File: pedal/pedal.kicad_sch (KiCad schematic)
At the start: 55 parts, among them J1 AudioJack3, J2 AudioJack3, J3 Micro SD, J4 USB_B_Micro, J5 Debug, U1 LP2985-1.8, U2 PCM3060, U3 TPS62172DSG, U4 TL072, U5 STM32H750IBTx, U6 RC4580, Y1 25MHz

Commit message: update JOURNAL and step down BC
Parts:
- added C37: 100nF, symbol Device:C
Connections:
- net +3V3: no longer C1.1, C10.2, C11.2, C12.2, C13.2, C14.2, C15.2, C16.2, C17.2, C2.1, C21.2, C24.1, C25.1, C26.2, C27.2, C28.2, C29.2, C3.2, C30.1, C30.2, C33.2, C34.2, C4.2, C5.2, C6.2, C7.2, C8.2, C9.2, J4.5 (GND), QSPI.10 (GND), SDRAM.12 (GNDQ), SDRAM.28 (GND), SDRAM.41 (GND), SDRAM.46 (GNDQ), SDRAM.52 (GNDQ), SDRAM.54 (GND), SDRAM.6 (GNDQ), U1.2 (GND), U2.8 (DGND), U3.1 (PGND), U3.2 (VIN), U3.3 (EN), U3.4 (AGND), U3.5 (FB), U5.102 (VSS), U5.113 (VSS), U5.126 (VSS), U5.135 (VSS), U5.14 (VSS), U5.148 (VSS), U5.158 (VSS), U5.22 (VSS), U5.48 (VSS), U5.61 (VSS), U5.71 (VSS), U5.90 (VSS)
- net at U2.21 (V_{COM}): now also C37.1
- net GNDA renamed +9V
- net +9V: now also C29.2, C30.1, C30.2, U3.1 (PGND), U3.2 (VIN), U3.3 (EN), U3.4 (AGND), U3.5 (FB), C37.2
- new net GNDD: C1.1, C10.2, C11.2, C12.2, C13.2, C14.2, C15.2, C16.2, C17.2, C2.1, C21.2, C24.1, C25.1, C26.2, C27.2, C28.2, C3.2, C33.2, C34.2, C4.2, C5.2, C6.2, C7.2, C8.2, C9.2, J4.5 (GND), QSPI.10 (GND), SDRAM.12 (GNDQ), SDRAM.28 (GND), SDRAM.41 (GND), SDRAM.46 (GNDQ), SDRAM.52 (GNDQ), SDRAM.54 (GND), SDRAM.6 (GNDQ), U1.2 (GND), U2.8 (DGND), U5.102 (VSS), U5.113 (VSS), U5.126 (VSS), U5.135 (VSS), U5.14 (VSS), U5.148 (VSS), U5.158 (VSS), U5.22 (VSS), U5.48 (VSS), U5.61 (VSS), U5.71 (VSS), U5.90 (VSS)
- no-connect marks 1 -> 3
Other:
- moved on the sheet: J3, J4, J5, L1, U1, U2, U3

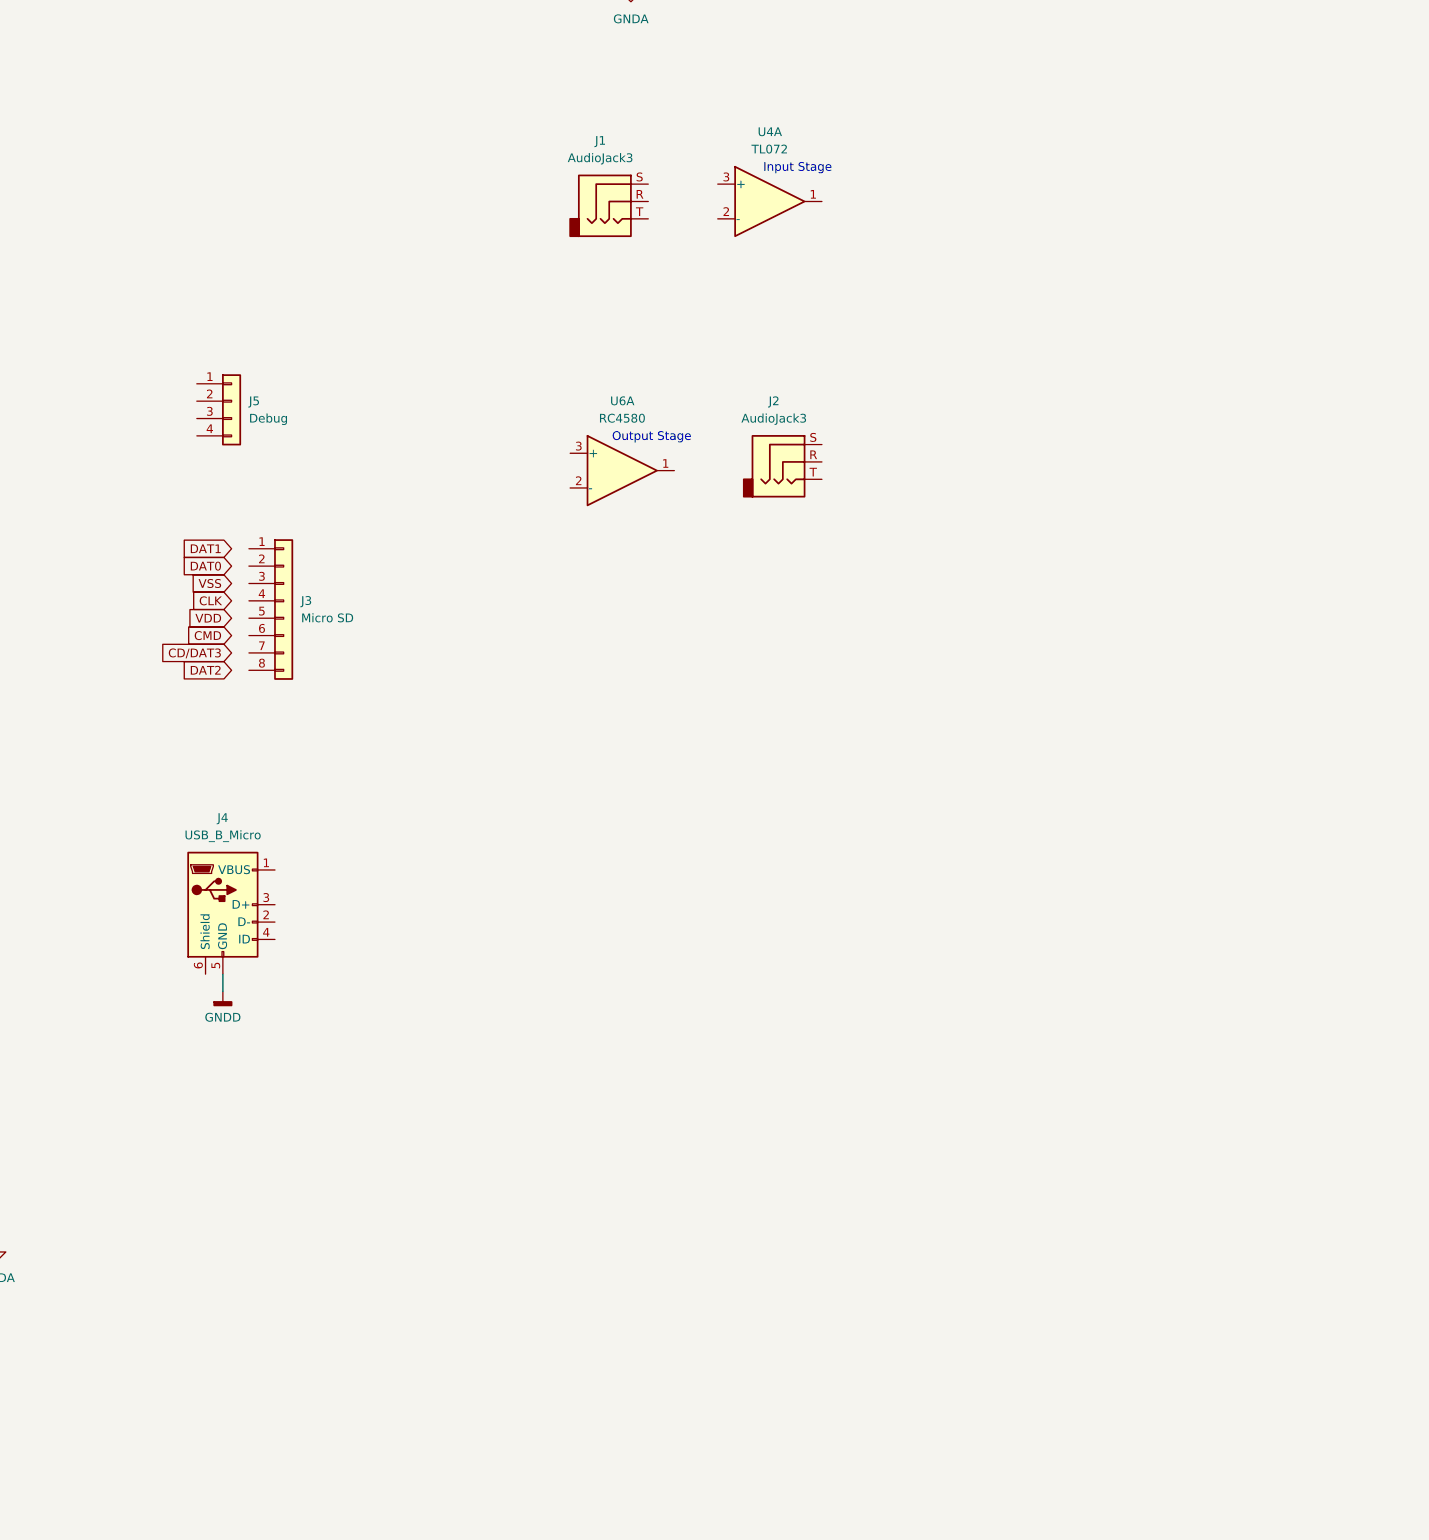
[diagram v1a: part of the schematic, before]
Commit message: consider differential inputs and outputs
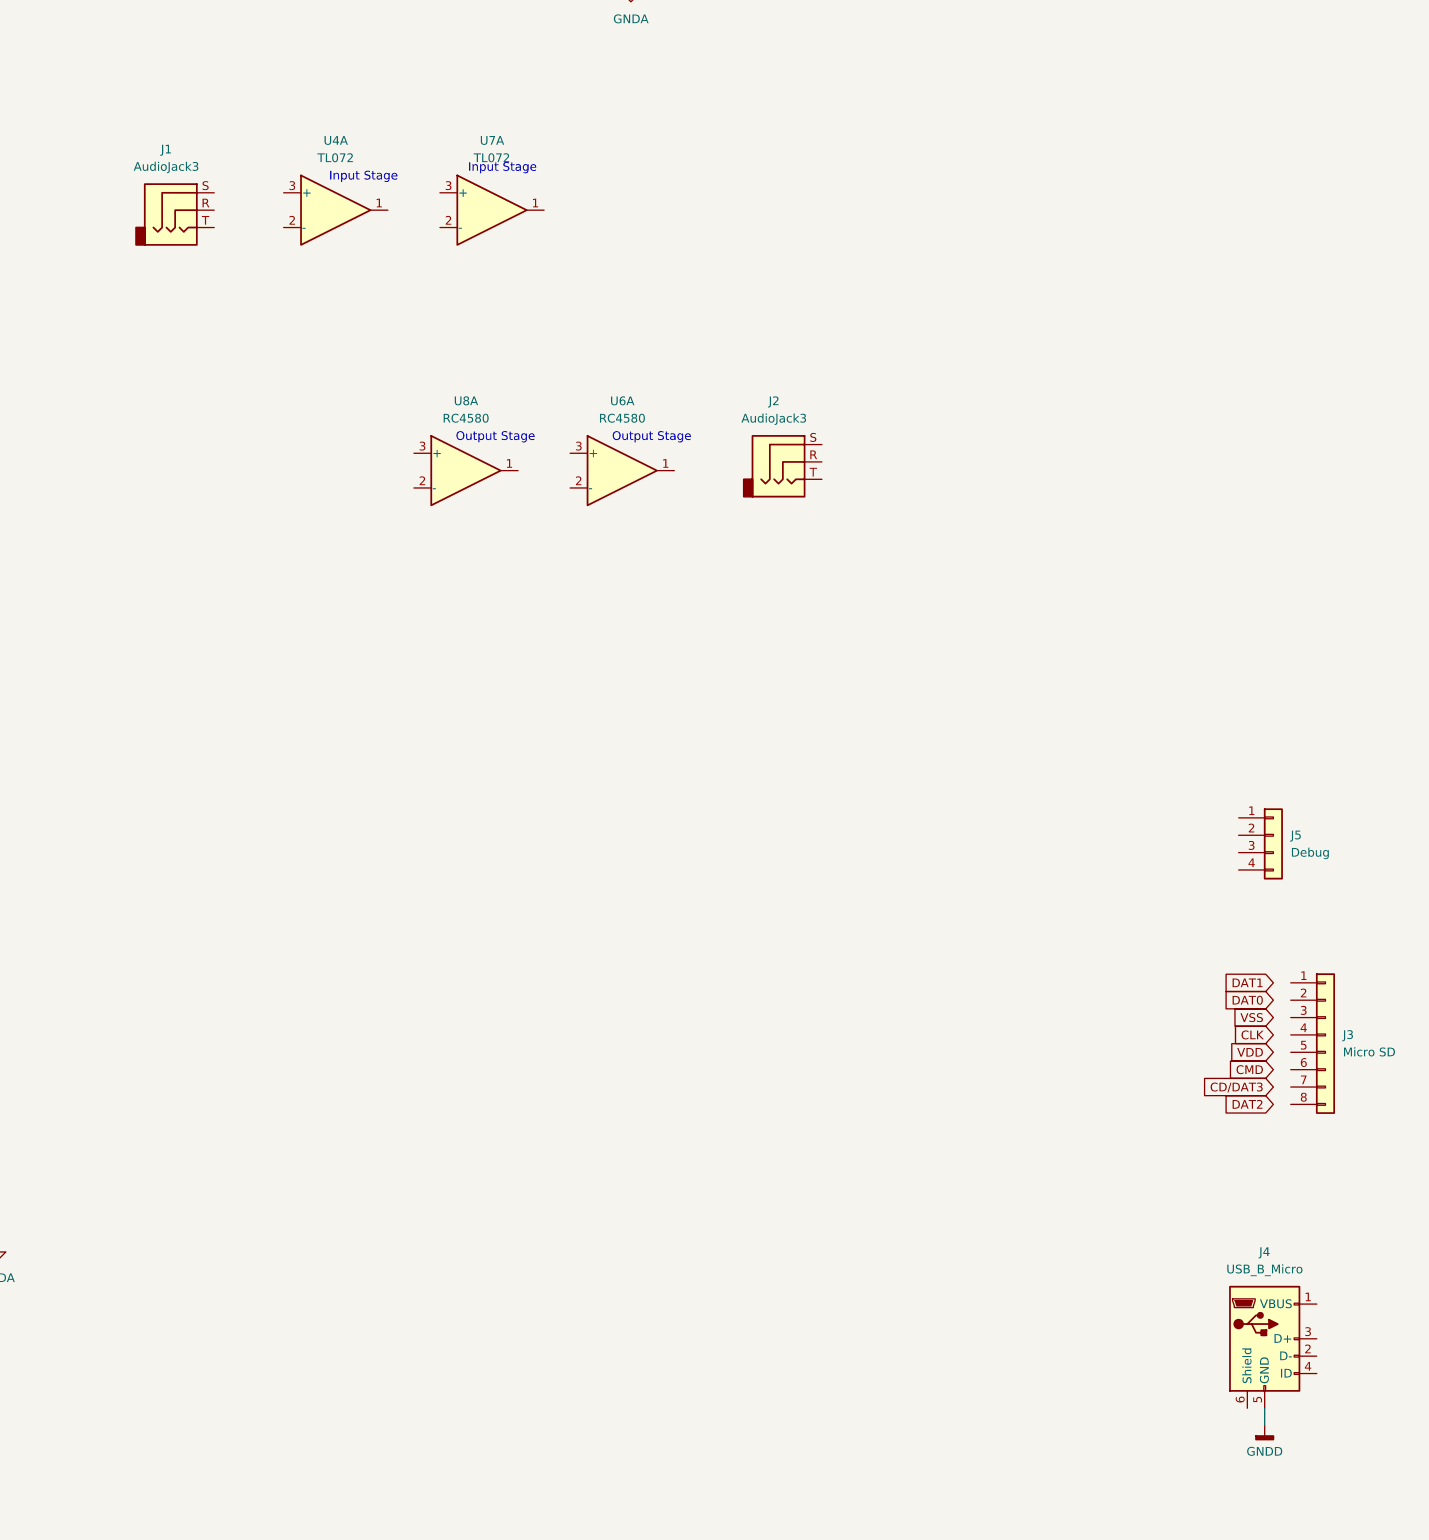
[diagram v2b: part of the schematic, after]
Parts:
- added U7: TL072, symbol Amplifier_Operational:TL072
- added U8: RC4580, symbol Amplifier_Operational:RC4580
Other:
- moved on the sheet: J1, J3, J4, J5, U4A

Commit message: Update simulation & dual op amps
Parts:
- removed U4, U7: TL072, symbol Amplifier_Operational:TL072
- removed U6: RC4580, symbol Amplifier_Operational:RC4580
- added C38: 1uF, symbol Device:C
- added C39, C40: 4.7uF, symbol Device:C
- added C41, C44: 10uF, symbol Device:C
- added C42: 2.2uF, symbol Device:C
- added C43: 10nF, symbol Device:C
- added C45: 330pF, symbol Device:C
- added C46: 0.1uF, symbol Device:C
- added C47: C, symbol Device:C
- added R10, R11, R14, R5: R, symbol Device:R
- added R12: 20k, symbol Device:R
- added R13, R6, R8: 10k, symbol Device:R
- added R4: 1k, symbol Device:R
- added R7, R9: 820, symbol Device:R
- added U4: LM27761, Package_SON:WSON-8-1EP_2x2mm_P0.5mm_EP0.9x1.6mm, symbol Regulator_SwitchedCapacitor:LM27761
- added U6: TL072, symbol Amplifier_Operational:TL072
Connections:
- net +3V3: no longer C35.1, C36.1, U2.24 (V_{CC})
- net +9V: now also J1.S, C39.2, C40.2, C41.1, C42.2, C46.2, R11.2, U4.2 (GND)
- net at U8.1: now also R5.1
- net at U8.2 (-): now also R9.2
- net at U8.3 (+): now also R7.2
- net INPUT: now reaches J1.T
- net INPUT: now also C47.1
- net at C37.1, U2.21 (V_{COM}): now also C41.2
- net VoutL-: now reaches U2.19 (V_{OUT}L-)
- net VoutL-: now also R6.1
- net VoutL+: now reaches U2.20 (V_{OUT}L+)
- net VoutL+: now also R8.1
- net VinL: now reaches U2.25 (V_{IN}L)
- net VinL: now also R14.2
- new net: C47.2, U6.3 (+)
- new net: C43.2, R8.2, R9.1
- new net: C40.1, U4.3 (CPOUT)
- new net: C42.1, R10.1, U4.4 (VOUT)
- new net: R10.2, R11.1, U4.5 (VFB)
- new net: C38.2, U4.7 (C-)
- new net: C38.1, U4.8 (C+)
- new net: C44.1, U6.1, U6.2 (-)
- new net: C44.2, R12.1
- new net: C43.1, R6.2, R7.1
- new net: C46.1, U6.6 (-)
- new net: C45.1, R12.2, R13.1, U6.5 (+)
- new net: C45.2, R13.2, R14.1, U6.7
- new net +5V: C35.1, C36.1, C39.1, U2.24 (V_{CC}), U4.1 (VIN)
- new net OUTPUT: R5.2
- no-connect marks 3 -> 4
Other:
- note added: "remember to add vcom"
- moved on the sheet: J1, J2, U8A

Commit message: finish wiring op amps
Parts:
- removed J3: Micro SD, symbol Connector_Generic:Conn_01x08
- removed J5: Debug, symbol Connector_Generic:Conn_01x04
- removed R5: R, symbol Device:R
- removed U8: RC4580, symbol Amplifier_Operational:RC4580
- added C48, C49: 470pF, symbol Device:C
- added C50, C51, C52, C53: 0.1uF, symbol Device:C
- added D1, D2: D, symbol Device:D
- added FB2: 120, symbol Device:FerriteBead_Small
- added R15: 7.5k, symbol Device:R
- added R16: 100, symbol Device:R
- added U7: RC4580, symbol Amplifier_Operational:RC4580
- C43: value 10nF -> 1500pF
- R10: value R -> 137k
- R11: value R -> 51.1k
- R4: value 1k -> 7.5k
- renumbered QSPI to QSPI1, SDRAM to SDRAM1
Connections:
- net +9V is gone; now on net +5V: C19.2, C20.2, C29.2, C30.1, C30.2, C35.2, C36.2, C37.2, C39.2, C40.2, C41.1, C42.2, C46.2, J1.S, R11.2, U2.16 (SGND), U2.22 (AGND2), U2.23 (AGND1), U3.1 (PGND), U3.2 (VIN), U3.3 (EN), U3.4 (AGND), U3.5 (FB), U3.9 (PAD), U4.2 (GND), U5.37 (VSSA)
- net +5V: now also J2.S, J4.1 (VBUS), R4.2, U4.9 (PAD), U6.8 (V+), C49.2, C50.1, C50.2, C51.2, C52.2, C53.1, C53.2, D1.2 (A), D2.1 (K), FB2.1, U7.5 (+), U7.8 (V+); no longer C39.1, U4.1 (VIN)
- net GNDD: now also J4.6 (Shield)
- net OUTPUT: now also J2.T, R16.2, U7.6 (-), U7.7
- net VinL: now also D1.1 (K), D2.2 (A)
- net at R4.1: now also C43.2, R8.2, R9.1
- net at R9.2: now also C49.1, U7.2 (-)
- net -4V5: now reaches C42.1, R10.1, U4.4 (VOUT)
- net -4V5: now also U6.4 (V-), C51.1, C52.1, U7.4 (V-)
- net at U4.6 (EN): now also C39.1, U4.1 (VIN), FB2.2
- net at C43.1, R6.2, R7.1: now also R15.1
- net at C46.1: now also U6.5 (+); no longer U6.6 (-)
- net at C45.1, R12.2, R13.1: now also U6.6 (-); no longer U6.5 (+)
- net PA11: now reaches J4.2 (D-)
- net PA11: now also U5.122 (PA11)
- net PA12: now reaches J4.3 (D+)
- net PA12: now also U5.123 (PA12)
- net at R7.2: now also C48.1, U7.3 (+)
- new net: C48.2, R15.2, R16.1, U7.1
- no-connect marks 4 -> 100
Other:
- note removed: "Output Stage"
- moved on the sheet: C38, C39, C40, C41, C42, C44, C45, C46, C47, J1, J2, J4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
